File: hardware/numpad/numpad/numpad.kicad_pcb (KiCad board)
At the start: 4 copper layers, 123.8 x 142.9 mm, 119 parts, among them IC1 LD1117-3.3V-SOT223, J1 Conn_01x06, SW1 ROT_SKYLOONG_HS, SW2 Push_Button, Y1 8MHz

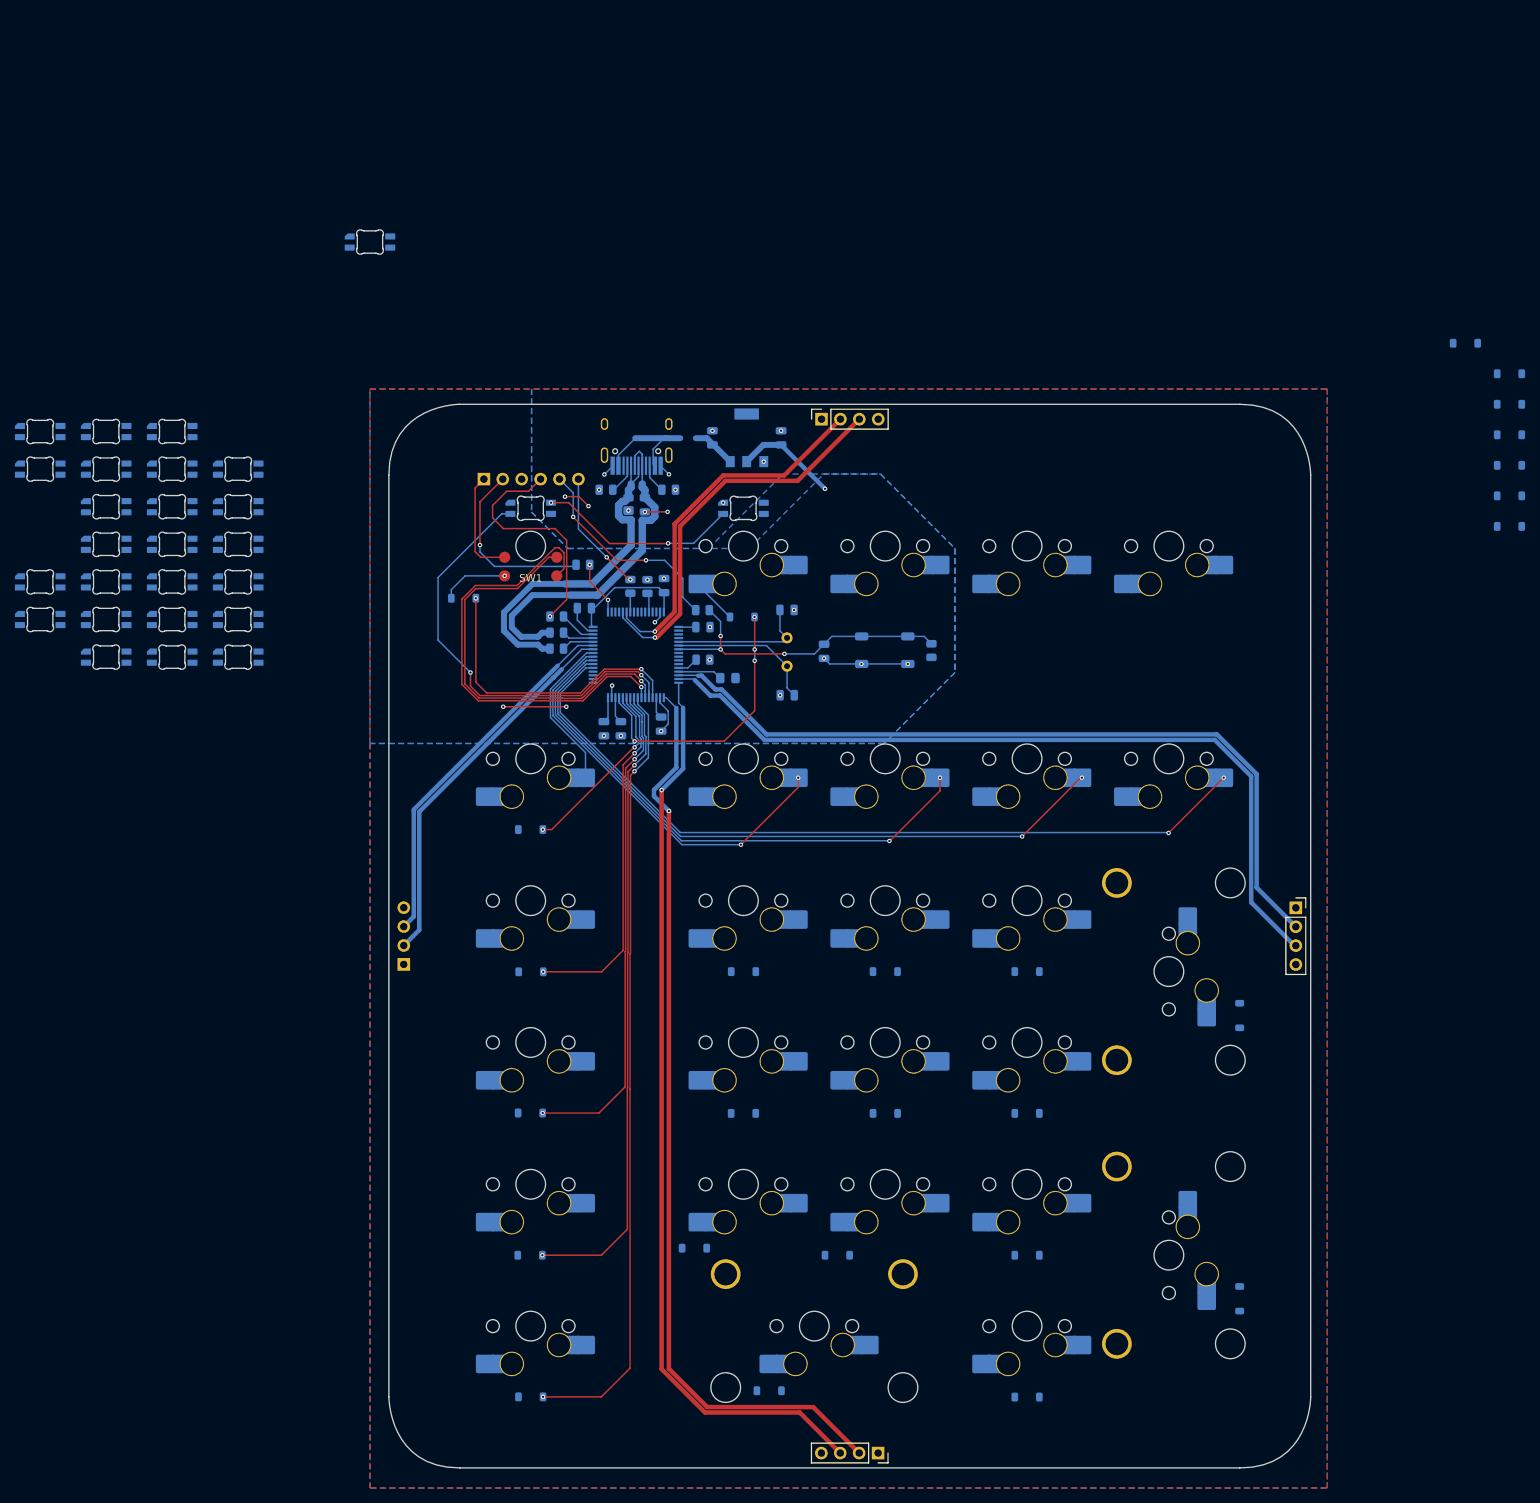
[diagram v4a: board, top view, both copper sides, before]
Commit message: LEDs
Placed all LEDs
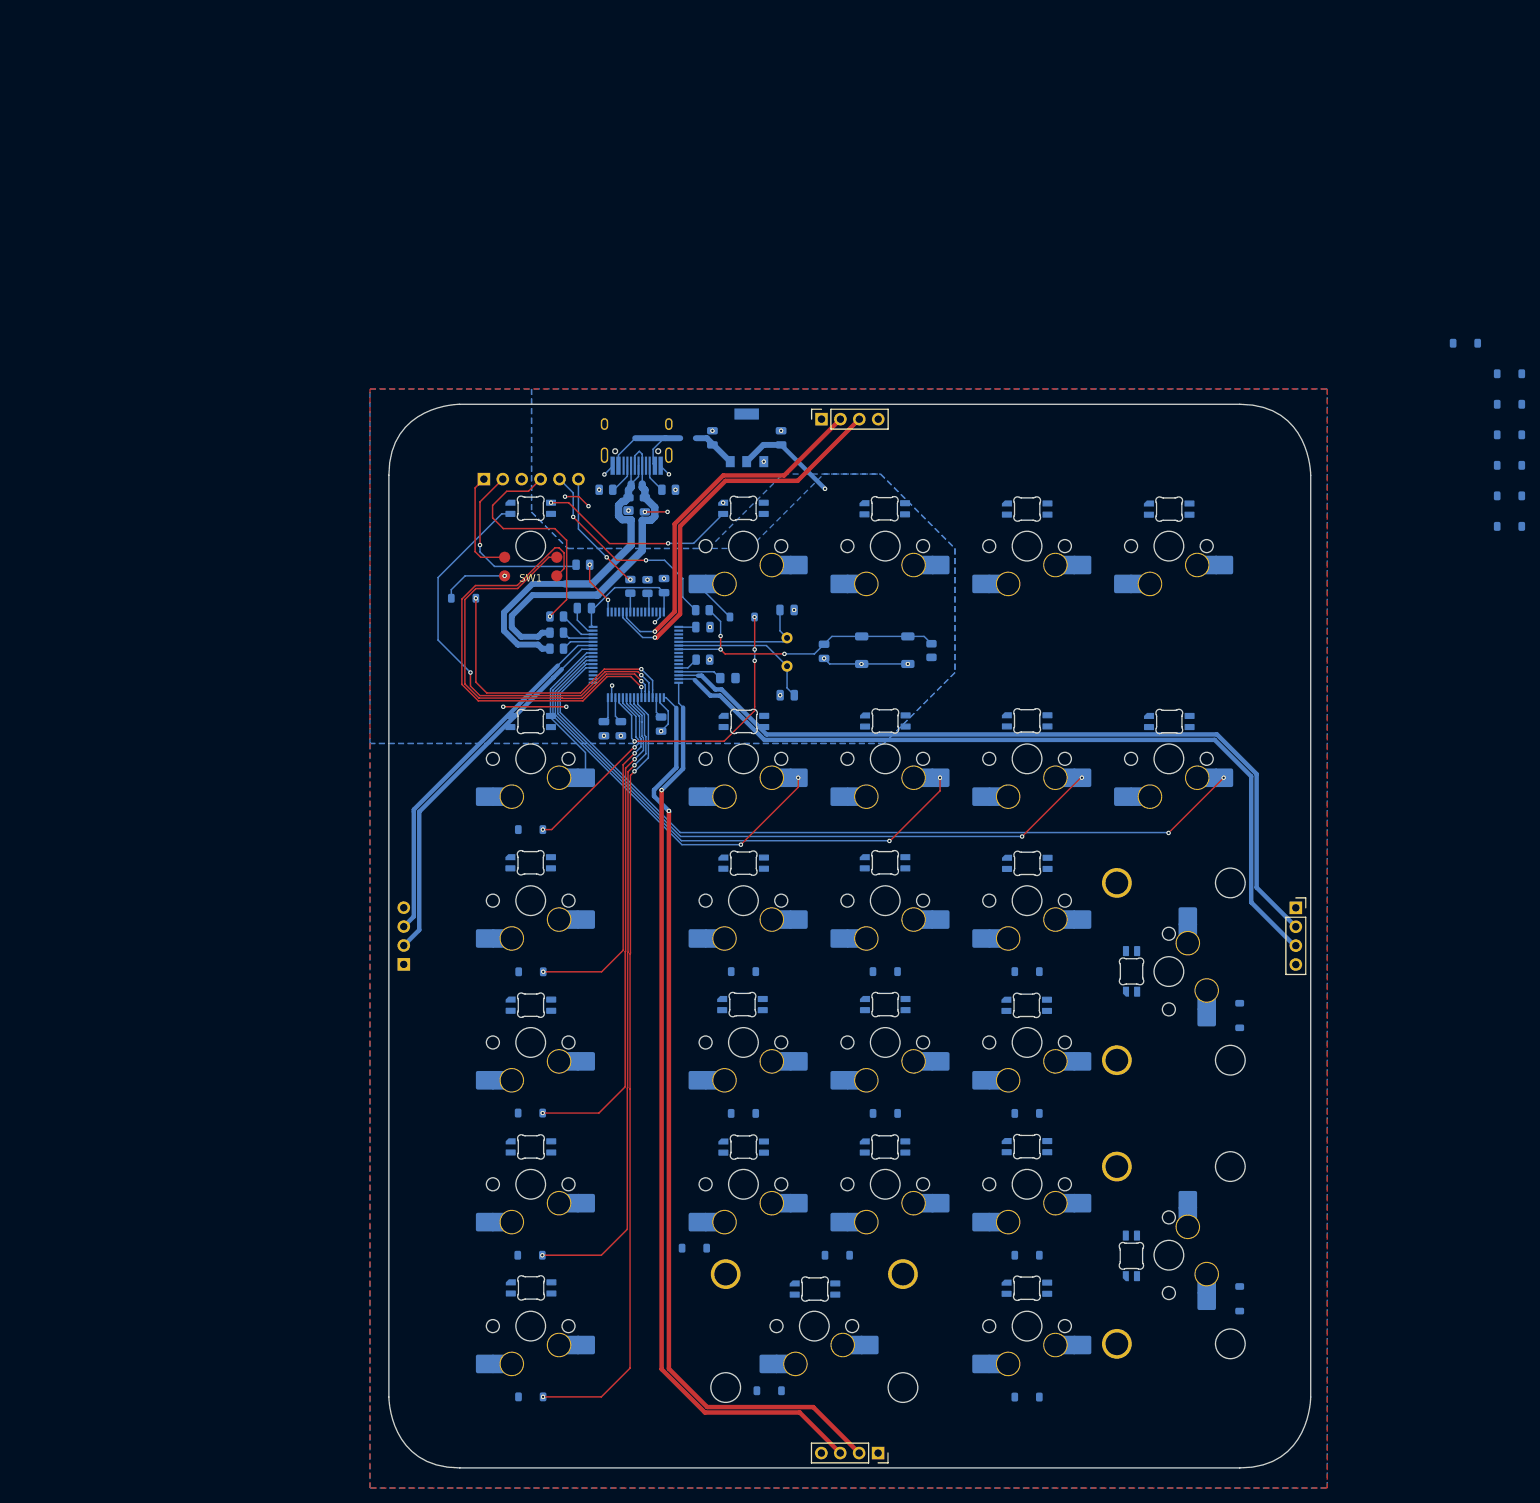
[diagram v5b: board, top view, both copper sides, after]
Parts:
- moved LED25 153.4 mm to (130.9, 156.9), turned to 90 degrees
- moved LED27 152.7 mm to (116.8, 161.3)
- moved LED11 149.2 mm to (130.9, 118.7), turned to 90 degrees
- moved LED10 144.0 mm to (135.9, 85.2)
- moved LED20 139.9 mm to (88.4, 161.4)
- moved LED2 133.4 mm to (116.9, 56.6)
- moved LED19 132.9 mm to (116.8, 123.3)
- moved LED12 132.7 mm to (116.9, 104.2)
- moved LED24 130.3 mm to (116.8, 142.3)
- moved LED9 124.5 mm to (116.9, 85.1)
- moved LED13 117.2 mm to (97.8, 104.1)
- moved LED18 114.0 mm to (97.8, 123.2)
- moved LED3 113.9 mm to (97.7, 56.6)
- moved LED1 113.2 mm to (135.9, 56.6)
- moved LED23 112.1 mm to (97.8, 142.3)
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
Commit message: pcb design draft
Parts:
- D1: footprint PCM_Package_TO_SOT_SMD_AKL:SOT-143 -> PCM_Package_TO_SOT_SMD_AKL:SOT-143_Handsoldering
- IC1: value LD1117-3.3V-SOT223 -> LD1117
- moved D7 105.8 mm to (86.8, 97.8)
- moved D4 89.7 mm to (97.7, 70.2)
- moved D8 87.0 mm to (105.9, 97.8)
- moved D10 75.6 mm to (127.2, 92.2), turned to 90 degrees
- moved D5 70.4 mm to (116.8, 70.2)
- moved D9 68.7 mm to (125.0, 97.7)
- moved D6 51.4 mm to (135.9, 70.2)
- moved R10 35.1 mm to (107.4, 85.1), turned to 90 degrees
- moved D14 22.2 mm to (124.0, 118.7), turned to 0 degrees
- moved D21 19.9 mm to (126.3, 156.8)
- moved D19 6.85 mm to (98.1, 155.7)
- moved D18 6.55 mm to (78.7, 155.8)
- moved D22 6.17 mm to (88.3, 175.9)
- moved D29 5.80 mm to (46.6, 70.5), turned to 90 degrees
- moved C2 4.97 mm to (88.9, 79.1), turned to 0 degrees
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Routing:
- net /COL2: track 55.3 -> 163.3 mm, vias 2 -> 9
- net /COL4: track 89.7 -> 190.3 mm, vias 2 -> 9
- net /COL5: track 107.3 -> 194.0 mm, vias 2 -> 4
- net /COL3: track 73.2 -> 152.9 mm, vias 2 -> 8
- net /ROW2: track 24.7 -> 102.4 mm, vias 2 -> 4
- net /COL1: track 21.6 -> 95.3 mm, vias 0 -> 5
- net /ROW5: track 86.0 -> 153.8 mm
- net /ROW3: track 47.7 -> 111.9 mm
- net /ROW6: track 105.0 -> 163.0 mm
- net /ROW1: track 37.2 -> 86.9 mm, vias 4 -> 3
- net Net-(LED20-DOUT): track 0.00 -> 47.8 mm
- net Net-(LED1-DOUT): track 0.00 -> 46.3 mm
- net Net-(LED16-DIN): track 0.00 -> 41.0 mm
- net Net-(LED20-DIN): track 0.00 -> 40.4 mm
- net Net-(LED6-DIN): track 0.00 -> 39.7 mm, vias 0 -> 2
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- added copper zone on In2.Cu, net +3.3V
- added copper zone on In2.Cu, net +5V
- added copper zone on In1.Cu, net AGND
- added copper zone on In1.Cu, net GND
- removed copper zone on B.Cu, net +3.3V
- removed copper zone on B.Cu, net +5V
- removed copper zone on F.Cu, net GND
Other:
- outline, holes or cut-outs redrawn
- board text added: "${REFERENCE}"

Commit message: bom list and some minor changes
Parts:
- IC1: value LD1117 -> LD1117-3.3V-SOT223
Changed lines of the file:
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@@
 			)
 		)
-		(property "Value" "LD1117"
+		(property "Value" "LD1117-3.3V-SOT223"
 			(at -10.825 -3.95 0)
 			(layer "B.SilkS")
@@
 		(tags "cherry MX 6028 rearmount rear mount led rgb backlight")
 		(property "Reference" "LED11"
-			(at 0 -2.6 90)
+			(at -5.4775 0.015001 180)
 			(layer "B.SilkS")
 			(effects
@@
 		(descr "Footprint for Cherry MX style switches with Kailh hotswap socket")
 		(property "Reference" "NUM_ENTER1"
-			(at 0 -3.515 90)
+			(at -7.775 -1.67 180)
 			(layer "B.SilkS")
 			(effects
@@
 		(tags "cherry MX 6028 rearmount rear mount led rgb backlight")
 		(property "Reference" "LED23"
-			(at 0 -2.6 0)
+			(at -6.315 -0.11 0)
 			(layer "B.SilkS")
 			(effects
@@
 		(tags "SOD-123")
 		(property "Reference" "D17"
-			(at 0 2.127 0)
+			(at -3.5 -0.01 90)
 			(layer "B.SilkS")
 			(effects
@@
 		(tags "SOD-123")
 		(property "Reference" "D23"
-			(at 0 2.127 0)
+			(at -3.42 -0.01 90)
 			(layer "B.SilkS")
 			(effects
@@
 		(descr "Footprint for Cherry MX style switches with Kailh hotswap socket")
 		(property "Reference" "MACRO_I1"
-			(at -2.54 -4.745 0)
+			(at -6.475 1.78 0)
 			(layer "B.SilkS")
 			(effects
@@
 		(tags "SOD-123")
 		(property "Reference" "D15"
-			(at 0 2.127 0)
+			(at -3.24 -0.03 90)
 			(layer "B.SilkS")
 			(effects
@@
 		(tags "cherry MX 6028 rearmount rear mount led rgb backlight")
 		(property "Reference" "LED26"
-			(at 0 -2.6 0)
+			(at -6.65 -0.04 0)
 			(layer "B.SilkS")
 			(effects
@@
 		(tags "cherry MX 6028 rearmount rear mount led rgb backlight")
 		(property "Reference" "LED24"
-			(at 0 -2.6 0)
+			(at -5.985 -0.03 0)
 			(layer "B.SilkS")
 			(effects
@@
 		(tags "cherry MX 6028 rearmount rear mount led rgb backlight")
 		(property "Reference" "LED16"
-			(at 0 -2.6 0)
+			(at -5.955 0.02 0)
 			(layer "B.SilkS")
 			(effects
@@
 		(tags "SOD-123")
 		(property "Reference" "D21"
-			(at 0 2.127 90)
+			(at -3.13 -0.07 180)
 			(layer "B.SilkS")
 			(effects
@@
 		(tags "cherry MX 6028 rearmount rear mount led rgb backlight")
 		(property "Reference" "LED17"
-			(at 0 -2.6 0)
+			(at -6.36 -0.07 180)
 			(layer "B.SilkS")
 			(effects
@@
 		(tags "cherry MX 6028 rearmount rear mount led rgb backlight")
 		(property "Reference" "LED25"
-			(at 0 -2.6 90)
+			(at -4.685 0.035 0)
 			(layer "B.SilkS")
 			(effects
@@
 		(tags "SOD-123")
 		(property "Reference" "D12"
-			(at 0 2.127 0)
+			(at -3.26 -0.07 90)
 			(layer "B.SilkS")
 			(effects
@@
 		(tags "SOD-123")
 		(property "Reference" "D25"
-			(at 0 2.127 0)
+			(at -3.36 -0.015 90)
 			(layer "B.SilkS")
 			(effects
@@
 		(tags "cherry MX 6028 rearmount rear mount led rgb backlight")
 		(property "Reference" "LED22"
-			(at 0 -2.6 0)
+			(at -6.41 -0.09 0)
 			(layer "B.SilkS")
 			(effects
@@
 		(descr "Footprint for Cherry MX style switches with Kailh hotswap socket")
 		(property "Reference" "NUM_ADD1"
-			(at 0 -3.965 90)
+			(at 5.225 -5.37 180)
 			(layer "B.SilkS")
 			(effects
@@
 		(tags "cherry MX 6028 rearmount rear mount led rgb backlight")
 		(property "Reference" "LED21"
-			(at 0 -2.6 0)
+			(at -6.68 -0.05 0)
 			(layer "B.SilkS")
 			(effects
@@
 		(tags "SOD-123")
 		(property "Reference" "D27"
-			(at 0 2.127 0)
+			(at -3.285 -0.01 90)
 			(layer "B.SilkS")
 			(effects
@@
 		(tags "SOD-123")
 		(property "Reference" "D26"
-			(at 0 2.127 0)
+			(at -3.265 0 90)
 			(layer "B.SilkS")
 			(effects
@@
 		(tags "SOD-123")
 		(property "Reference" "D18"
-			(at 0 2.127 0)
+			(at -3.28 0 90)
 			(layer "B.SilkS")
 			(effects
@@
 		(tags "cherry MX 6028 rearmount rear mount led rgb backlight")
 		(property "Reference" "LED19"
-			(at 0 -2.6 0)
+			(at -6.33 0.03 180)
 			(layer "B.SilkS")
 			(effects
@@
 		(descr "Footprint for Cherry MX style switches with Kailh hotswap socket")
 		(property "Reference" "NUM_PERIOD1"
-			(at -2.54 -4.17 0)
+			(at -7.18 1.81 0)
 			(layer "B.SilkS")
 			(effects
@@
 		(tags "cherry MX 6028 rearmount rear mount led rgb backlight")
 		(property "Reference" "LED15"
-			(at 0 -2.6 0)
+			(at -6.03 0.02 0)
 			(layer "B.SilkS")
 			(effects
@@
 	(footprint "PCM_marbastlib-mx:SW_MX_HS_CPG151101S11_1u"
 		(layer "B.Cu")
-		(at 88.265 166.37)
+		(at 88.254824 166.33)
 		(descr "Footprint for Cherry MX style switches with Kailh hotswap socket")
 		(property "Reference" "NUM_0"
-			(at 0 -4.995 0)
+			(at -6.994824 1.9 0)
 			(layer "B.SilkS")
 			(effects
@@
 		(tags "SOD-123")
 		(property "Reference" "D16"
-			(at 0 2.127 0)
+			(at -3.45 -0.03 270)
 			(layer "B.SilkS")
 			(effects
@@
 		(tags "SOD-123")
 		(property "Reference" "D22"
-			(at 0 2.127 0)
+			(at -3.32 -0.01 270)
 			(layer "B.SilkS")
 			(effects
@@
 		(tags "cherry MX 6028 rearmount rear mount led rgb backlight")
 		(property "Reference" "LED18"
-			(at 0 -2.6 0)
+			(at -6.22 0.06 0)
 			(layer "B.SilkS")
 			(effects
@@
 		(tags "SOD-123")
 		(property "Reference" "D20"
-			(at 0 2.127 0)
+			(at -3.49 0 270)
 			(layer "B.SilkS")
 			(effects
@@
 		(tags "SOD-123")
 		(property "Reference" "D11"
-			(at 0 2.127 0)
+			(at -3.26 0 90)
 			(layer "B.SilkS")
 			(effects
@@
 		(tags "SOD-123")
 		(property "Reference" "D13"
-			(at 0 2.127 0)
+			(at -3.25 0.02 90)
 			(layer "B.SilkS")
 			(effects
@@
 		(tags "SOD-123")
 		(property "Reference" "D19"
-			(at 0 2.127 0)
+			(at -3.21 0.04 90)
 			(layer "B.SilkS")
 			(effects
@@
 		(tags "SOD-123")
 		(property "Reference" "D14"
-			(at 0 2.127 0)
+			(at 3.23 0.11 270)
 			(layer "B.SilkS")
 			(effects

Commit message: messages
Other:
- board text added: "ARHKEIA"
- board text added: "Team SKBD Numpad"
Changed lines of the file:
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@@
 		(tags "STM32F446RET6 ")
 		(property "Reference" "U1"
-			(at 0 0 0)
+			(at 0.14375 0.17 0)
 			(unlocked yes)
 			(layer "B.SilkS")
@@
 		(layer "Edge.Cuts")
 	)
+	(gr_text "Team SKBD\nNumpad"
+		(at 64.41 77.68 0)
+		(layer "F.SilkS")
+		(effects
+			(font
+				(size 1 1)
+				(thickness 0.25)
+				(bold yes)
+			)
+			(justify bottom)
+		)
+	)
+	(gr_text "ARHKEIA"
+		(at 139.8 169.55 -0)
+		(layer "B.SilkS")
+		(effects
+			(font
+				(size 1 1)
+				(thickness 0.15)
+			)
+			(justify left bottom mirror)
+		)
+	)
 	(gr_text "5VD\n"
